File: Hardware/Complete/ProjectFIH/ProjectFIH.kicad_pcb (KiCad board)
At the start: 2 copper layers, 84 parts, among them J1 Conn_01x02_Male, J10 Payload LED, J2 Power, J3 Power LED, J4 MCU Fail LED, J5 Heater LED, J6 Heater, J7 UART, J8 AVR-ISP-10, J9 Payload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

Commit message: Partially routed PCB
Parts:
- U6: footprint Package_SO:SOIC-8-1EP_3.9x4.9mm_P1.27mm_EP2.29x3mm -> Package_SO:SOIC-8_3.9x4.9mm_P1.27mm
- moved C13 176.0 mm to (221.5, 61.1), turned to 270 degrees
- moved C24 173.6 mm to (208.8, 63.6), turned to 270 degrees
- moved D6 159.8 mm to (226.2, 20.6), turned to 270 degrees
- moved J9 159.4 mm to (212.2, 19.4)
- moved U6 155.6 mm to (214.5, 63.0)
- moved C20 142.7 mm to (214.7, 59.2), turned to 180 degrees
- moved RV2 138.8 mm to (220.5, 39.7), turned to 90 degrees
- moved C16 136.4 mm to (221.5, 64.5), turned to 270 degrees
- moved J2 134.7 mm to (170.9, 20.1)
- moved L1 134.3 mm to (215.3, 55.9), turned to 180 degrees
- moved J10 131.8 mm to (222.4, 19.4)
- moved C9 130.9 mm to (170.2, 33.5)
- moved R23 127.7 mm to (223.6, 43.7), turned to 270 degrees
- moved R26 126.1 mm to (222.4, 15.6), turned to 90 degrees
- moved C22 121.6 mm to (210.1, 66.2), turned to 270 degrees
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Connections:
- J6 pad 1: +24V -> Net-(J5-Pad2)
- J6 pad 2: Net-(J5-Pad2) -> +24V
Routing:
- net GND: track 62.4 -> 288.2 mm, vias 0 -> 2
- net +24V: track 11.0 -> 158.7 mm
- net Net-(C23-Pad1): track 29.3 -> 101.4 mm
- net +5V: track 0.00 -> 67.8 mm
- net Net-(R23-Pad1): track 0.00 -> 38.4 mm
- net Net-(J5-Pad2): track 0.00 -> 23.2 mm
- net Net-(Q1-Pad3): track 0.00 -> 16.4 mm
- net Net-(C20-Pad1): track 0.00 -> 10.2 mm
- net Net-(J5-Pad1): track 0.00 -> 8.86 mm
- net Net-(D6-Pad1): track 0.00 -> 8.17 mm
- net PL_ON: track 0.00 -> 3.97 mm, vias 0 -> 1
- net Net-(Q1-Pad1): track 0.00 -> 3.90 mm
- net Net-(Q2-Pad1): track 0.00 -> 3.82 mm
- net Net-(J3-Pad1): track 0.00 -> 3.29 mm
- net Net-(R23-Pad2): track 0.00 -> 3.17 mm
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- added copper zone on F.Cu, net GND

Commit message: More tracing
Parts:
- Q3: footprint Package_TO_SOT_THT:TO-220-3_Vertical -> Package_TO_SOT_THT:TO-220-3_Horizontal_TabDown
- R16, R19: value 10k -> 47k
- moved J8 101.9 mm to (79.4, 102.9), turned to 270 degrees
- moved C18 91.9 mm to (55.2, 101.0), turned to 180 degrees
- moved C21 76.3 mm to (62.2, 89.5), turned to 90 degrees
- moved C15 73.3 mm to (55.0, 96.5), turned to 180 degrees
- moved Y1 57.7 mm to (60.3, 101.0), turned to 90 degrees
- moved C12 51.5 mm to (70.1, 81.3)
- moved U8 39.7 mm to (69.4, 89.1)
- moved C19 29.3 mm to (76.8, 89.9), turned to 90 degrees
- moved Q2 25.3 mm to (178.0, 52.9)
- moved R14 25.3 mm to (172.2, 57.0)
- moved R18 25.3 mm to (182.4, 53.0)
- moved Q1 25.3 mm to (178.1, 57.8)
- moved R17 25.3 mm to (172.2, 51.9)
- moved R16 25.3 mm to (175.3, 58.0)
- moved R19 25.3 mm to (175.3, 53.0)
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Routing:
- net MCUReset: track 0.00 -> 43.2 mm
- net GND: track 288.2 -> 326.1 mm
- net Net-(Q1-Pad3): track 16.4 -> 36.9 mm
- net Net-(J5-Pad2): track 23.2 -> 41.0 mm
- net Net-(J8-Pad1): track 0.00 -> 15.4 mm, vias 0 -> 1
- net Net-(C18-Pad1): track 0.00 -> 15.2 mm
- net Net-(C15-Pad1): track 0.00 -> 12.2 mm
- net Net-(J8-Pad7): track 0.00 -> 11.7 mm
- net +24V: track 158.7 -> 169.9 mm
- net Net-(J8-Pad9): track 0.00 -> 10.7 mm
- net +5V: track 67.8 -> 58.1 mm, vias 0 -> 4
- net MCUHeatOff: track 0.00 -> 8.86 mm, vias 0 -> 1
- net Net-(J5-Pad1): track 8.86 -> 3.24 mm
- net MCU_PL_ON: track 0.00 -> 4.43 mm, vias 0 -> 1
- net IRQResp: track 0.00 -> 4.34 mm, vias 0 -> 1
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- added copper zone on F.Cu, net Net-(J5-Pad2)

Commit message: More tracing
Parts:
- C4, C7: moved to B.Cu
- moved C12 101.3 mm to (171.2, 74.7)
- moved C15 101.3 mm to (156.1, 89.9)
- moved C21 101.3 mm to (163.3, 82.9)
- moved J8 101.3 mm to (180.5, 96.3)
- moved U8 101.3 mm to (170.5, 82.5)
- moved C19 101.3 mm to (177.9, 83.3)
- moved Y1 101.3 mm to (161.4, 94.4)
- moved C18 101.3 mm to (156.3, 94.4)
- moved R3 87.8 mm to (84.8, 101.6), turned to 270 degrees
- moved U5 81.2 mm to (101.8, 95.9), turned to 90 degrees
- moved C7 78.9 mm to (101.6, 95.8), turned to 270 degrees
- moved C3 76.0 mm to (79.2, 98.8), turned to 270 degrees
- moved D2 71.4 mm to (91.6, 101.6)
- moved U1 67.1 mm to (87.1, 95.9), turned to 90 degrees
- moved R12 66.3 mm to (88.1, 101.6), turned to 90 degrees
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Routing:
- net Net-(U1-Pad5): track 0.00 -> 42.8 mm
- net GND: track 326.1 -> 365.7 mm, vias 2 -> 4
- net +5V: track 58.1 -> 93.9 mm, vias 4 -> 6
- net Net-(C1-Pad1): track 0.00 -> 28.9 mm
- net Net-(C1-Pad2): track 0.00 -> 10.1 mm
- net Net-(C3-Pad2): track 0.00 -> 6.42 mm
- net Net-(R3-Pad1): track 0.00 -> 3.54 mm
- net Net-(R12-Pad2): track 0.00 -> 2.94 mm
- net Net-(D2-Pad1): track 0.00 -> 2.45 mm

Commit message: More tracing
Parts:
- C10: moved to B.Cu
- moved U3 62.5 mm to (100.8, 79.8), turned to 90 degrees
- moved D1 60.8 mm to (99.7, 87.6)
- moved C10 60.4 mm to (101.1, 79.2), turned to 270 degrees
- moved C5 46.8 mm to (95.5, 88.4), turned to 180 degrees
- moved R5 40.4 mm to (99.8, 90.4)
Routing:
- net Net-(C5-Pad1): track 0.00 -> 25.6 mm
- net +5V: track 93.9 -> 118.6 mm, vias 6 -> 7
- net GND: track 365.7 -> 381.5 mm, vias 4 -> 5
- net Net-(U1-Pad5): track 42.8 -> 57.1 mm
- net Net-(R13-Pad2): track 0.00 -> 8.00 mm
- net Net-(U2-Pad2): track 0.00 -> 1.27 mm

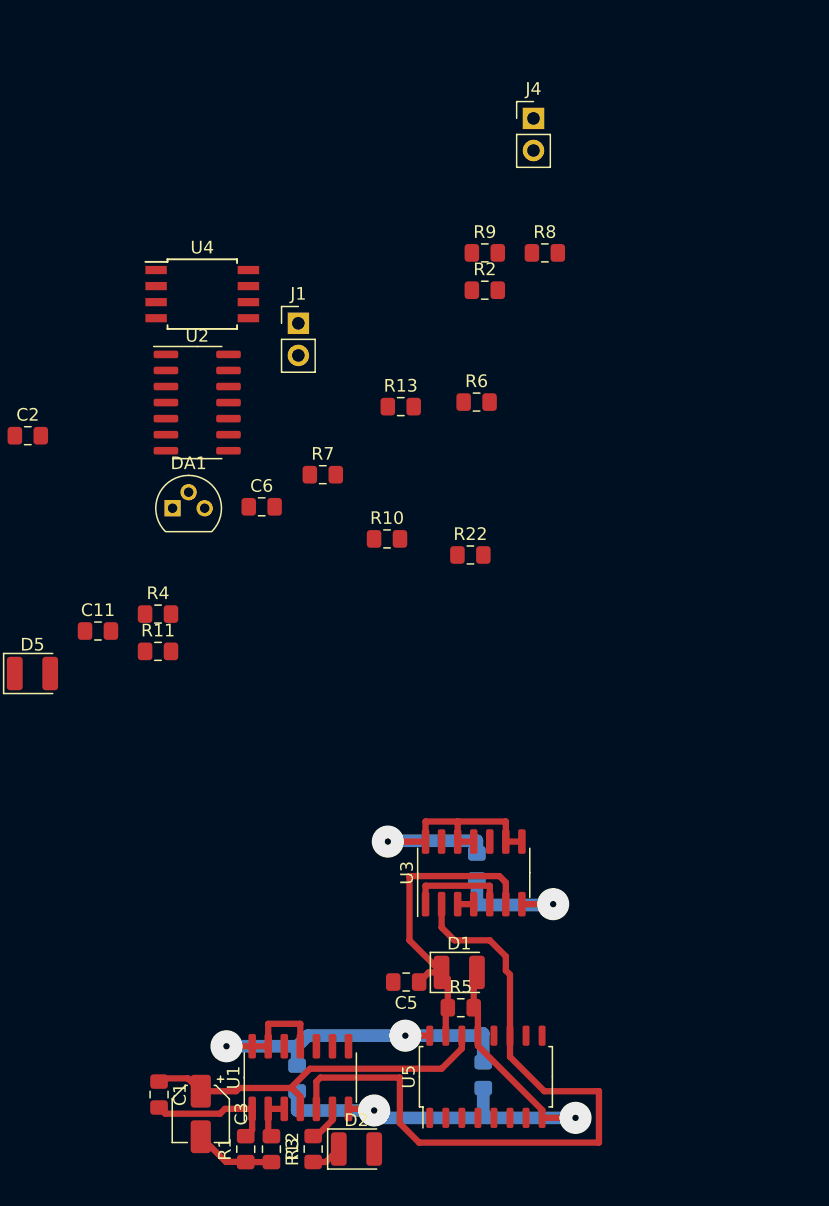
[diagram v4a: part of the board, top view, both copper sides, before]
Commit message: Before coupling MCU with hardware watchdog
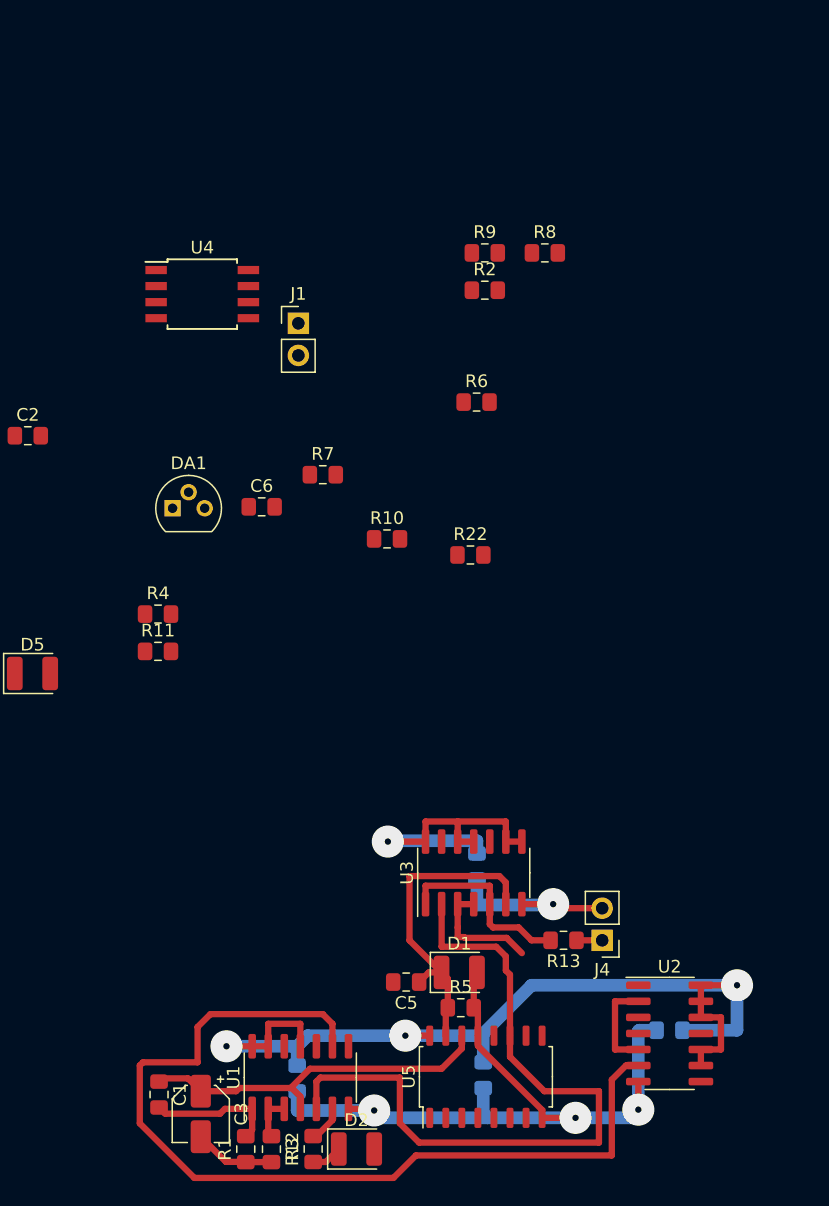
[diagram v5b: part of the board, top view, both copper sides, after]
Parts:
- C11: moved to B.Cu
- moved J4 65.2 mm to (111.0, 85.1), turned to 180 degrees
- moved U2 62.3 mm to (116.3, 92.5)
- moved C11 55.1 mm to (116.3, 92.2), turned to 180 degrees
- moved R13 44.1 mm to (107.9, 85.1), turned to 180 degrees
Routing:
- net Net-(U1-Pad9): track 0.00 -> 73.6 mm
- net +5V: track 118.6 -> 160.5 mm, vias 7 -> 8
- net GND: track 381.5 -> 400.7 mm, vias 5 -> 6
- net Net-(U2-Pad2): track 1.27 -> 17.0 mm
- net Net-(R13-Pad2): track 8.00 -> 14.9 mm
- net Net-(J4-Pad1): track 0.00 -> 2.03 mm
- net Net-(U1-Pad5): track 57.1 -> 58.0 mm

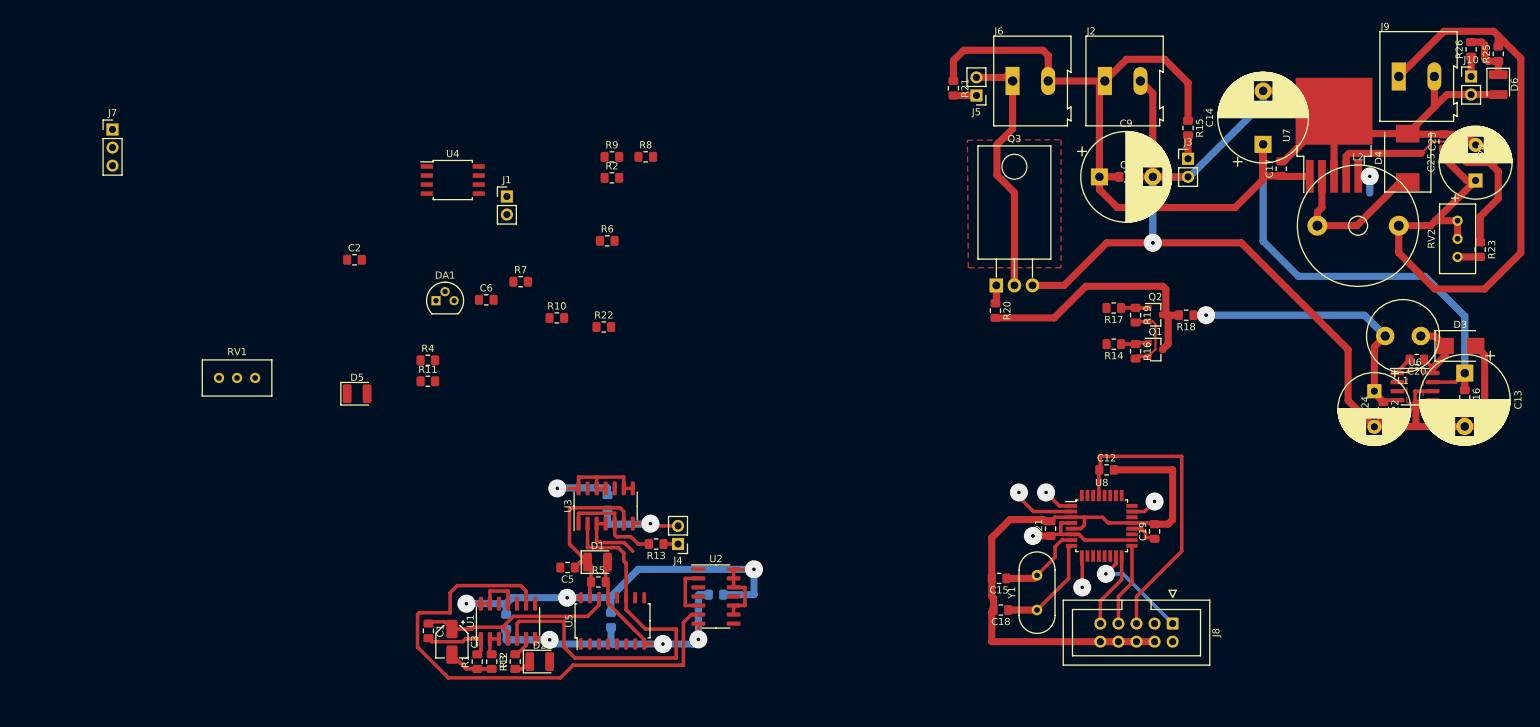
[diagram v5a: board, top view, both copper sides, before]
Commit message: MCU coupled with hardware watchdog
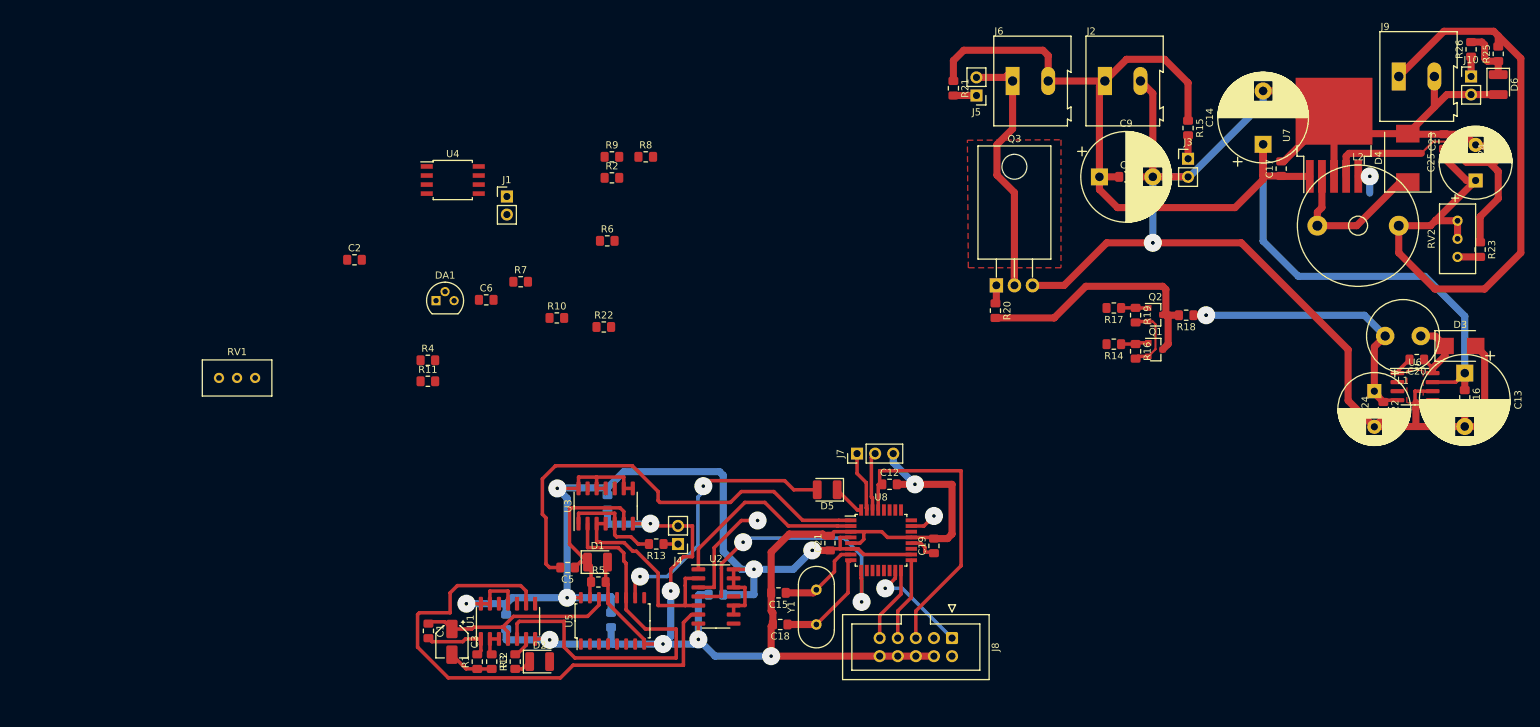
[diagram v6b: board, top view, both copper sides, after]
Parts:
- moved J7 114.0 mm to (136.1, 72.4), turned to 90 degrees
- moved D5 67.4 mm to (131.9, 77.5), turned to 180 degrees
- moved C15 31.1 mm to (125.1, 91.9)
- moved C19 31.1 mm to (146.9, 85.4)
- moved C21 31.1 mm to (132.3, 85.0)
- moved J8 31.1 mm to (149.5, 98.3)
- moved U8 31.1 mm to (139.5, 84.6)
- moved Y1 31.1 mm to (130.4, 96.4)
- moved C18 31.1 mm to (125.3, 96.4)
- moved C12 30.5 mm to (140.7, 76.7)
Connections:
- U8 pad 30: Net-(J7-Pad1) -> Net-(J7-Pad2)
- U8 pad 31: Net-(J7-Pad2) -> Net-(J7-Pad1)
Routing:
- net IRQResp: track 4.34 -> 63.6 mm, vias 1 -> 0
- net IRQ: track 0.00 -> 39.0 mm, vias 0 -> 2
- net GND: track 400.7 -> 438.0 mm, vias 6 -> 9
- net +5V: track 160.5 -> 197.6 mm
- net MCU_PL_ON: track 4.43 -> 40.9 mm, vias 1 -> 2
- net MCUHeatOff: track 8.86 -> 28.3 mm, vias 1 -> 0
- net HeatOFF: track 0.00 -> 15.5 mm, vias 0 -> 1
- net Net-(U2-Pad2): track 17.0 -> 30.2 mm
- net Net-(J7-Pad1): track 0.00 -> 8.49 mm
- net Net-(J7-Pad2): track 0.00 -> 8.21 mm
- net Net-(D5-Pad1): track 0.00 -> 4.54 mm

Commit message: Need to connect units
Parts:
- C6: moved to B.Cu
- moved R6 63.7 mm to (40.4, 23.1), turned to 270 degrees
- moved R8 62.9 mm to (44.2, 21.8), turned to 180 degrees
- moved R2 62.9 mm to (38.9, 35.3)
- moved R22 58.7 mm to (148.1, 89.2)
- moved R10 56.4 mm to (39.9, 37.3), turned to 180 degrees
- moved R7 53.0 mm to (40.4, 26.9), turned to 270 degrees
- moved R9 48.6 mm to (53.1, 31.8)
- moved R4 46.7 mm to (48.0, 21.8), turned to 180 degrees
- moved C6 44.3 mm to (47.3, 26.2), turned to 180 degrees
- moved J1 44.2 mm to (112.0, 72.6), turned to 90 degrees
- moved R11 42.6 mm to (52.6, 26.6), turned to 270 degrees
- moved DA1 38.4 mm to (42.9, 33.3), turned to 180 degrees
- moved U4 33.4 mm to (47.0, 25.9)
- moved C2 28.8 mm to (41.1, 30.0), turned to 180 degrees
- moved RV1 28.3 mm to (47.2, 33.8), turned to 180 degrees
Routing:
- net +5V: track 197.6 -> 264.2 mm, vias 8 -> 9
- net Net-(C5-Pad1): track 25.6 -> 71.5 mm
- net GND: track 438.0 -> 465.3 mm, vias 9 -> 10
- net Net-(R10-Pad1): track 0.00 -> 27.0 mm
- net Net-(R11-Pad2): track 0.00 -> 15.7 mm
- net Net-(C2-Pad1): track 0.00 -> 14.0 mm
- net Net-(R4-Pad2): track 0.00 -> 10.5 mm
- net Temperature: track 3.76 -> 11.9 mm, vias 1 -> 2
- net IRQ: track 39.0 -> 43.3 mm
- net Net-(R9-Pad1): track 0.00 -> 2.14 mm
- net Net-(R11-Pad1): track 0.00 -> 2.12 mm
- net MCUReset: track 43.2 -> 43.9 mm

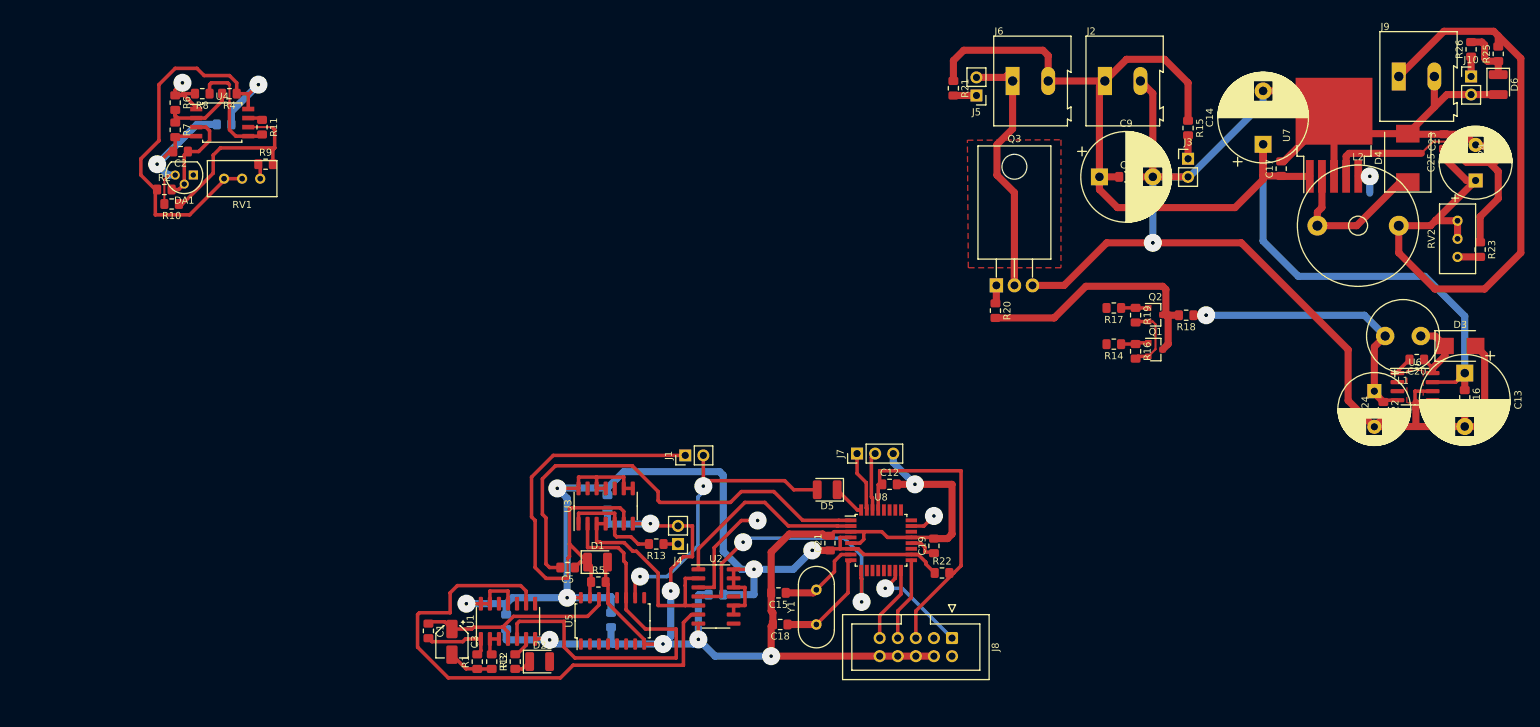
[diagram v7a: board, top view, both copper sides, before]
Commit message: Tracing done except widening and filling
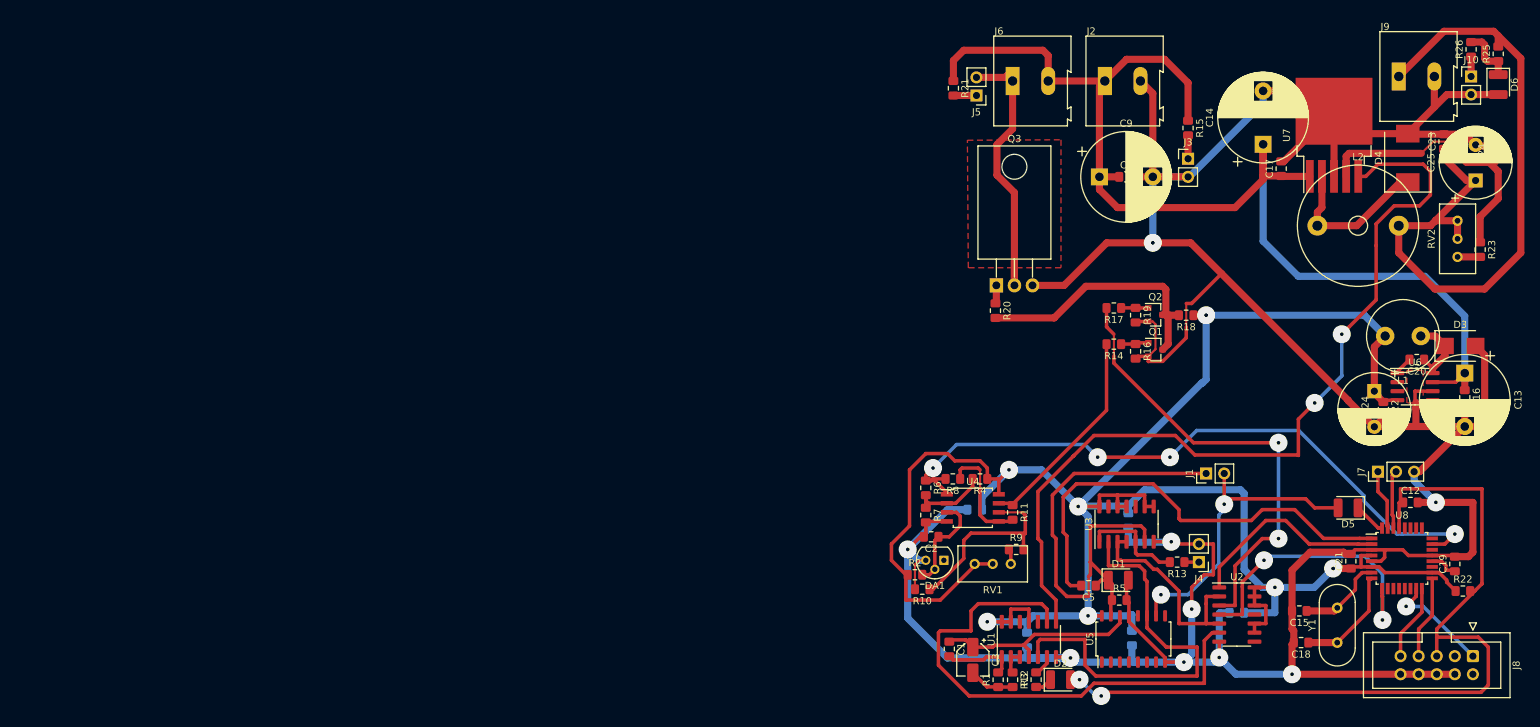
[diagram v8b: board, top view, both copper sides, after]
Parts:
- moved R2 118.5 mm to (144.3, 89.4)
- moved R9 118.5 mm to (158.5, 85.9)
- moved RV1 118.5 mm to (152.7, 87.9)
- moved U4 118.5 mm to (152.4, 80.0)
- moved C6 118.5 mm to (152.7, 80.3)
- moved DA1 118.5 mm to (148.3, 87.4)
- moved R4 118.5 mm to (153.4, 75.9)
- moved R8 118.5 mm to (149.6, 75.9)
- moved C2 118.5 mm to (146.5, 84.1)
- moved R10 118.5 mm to (145.3, 91.4)
- moved R11 118.5 mm to (158.0, 80.7)
- moved R6 118.5 mm to (145.8, 77.2)
- moved R7 118.5 mm to (145.8, 81.0)
- moved C1 73.2 mm to (149.1, 99.8)
- moved C12 73.2 mm to (213.9, 79.2)
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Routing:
- net PL_ON: track 3.97 -> 121.4 mm, vias 1 -> 2
- net Temperature: track 11.9 -> 95.4 mm, vias 2 -> 4
- net MCUReset: track 43.9 -> 117.3 mm, vias 0 -> 2
- net GND: track 465.3 -> 524.6 mm
- net HeatOFF: track 15.5 -> 64.9 mm, vias 1 -> 2
- net +5V: track 264.2 -> 310.4 mm
- net Net-(R11-Pad1): track 2.12 -> 30.1 mm
